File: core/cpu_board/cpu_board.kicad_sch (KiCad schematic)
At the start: 57 parts, among them J1 Data Low, J10 Cycle control, J11 CPU status, J12 CPU control, J13 Power, J2 Data High, J3 Address Low, J4 Address Mid, J5 Address High, J6 JTAG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

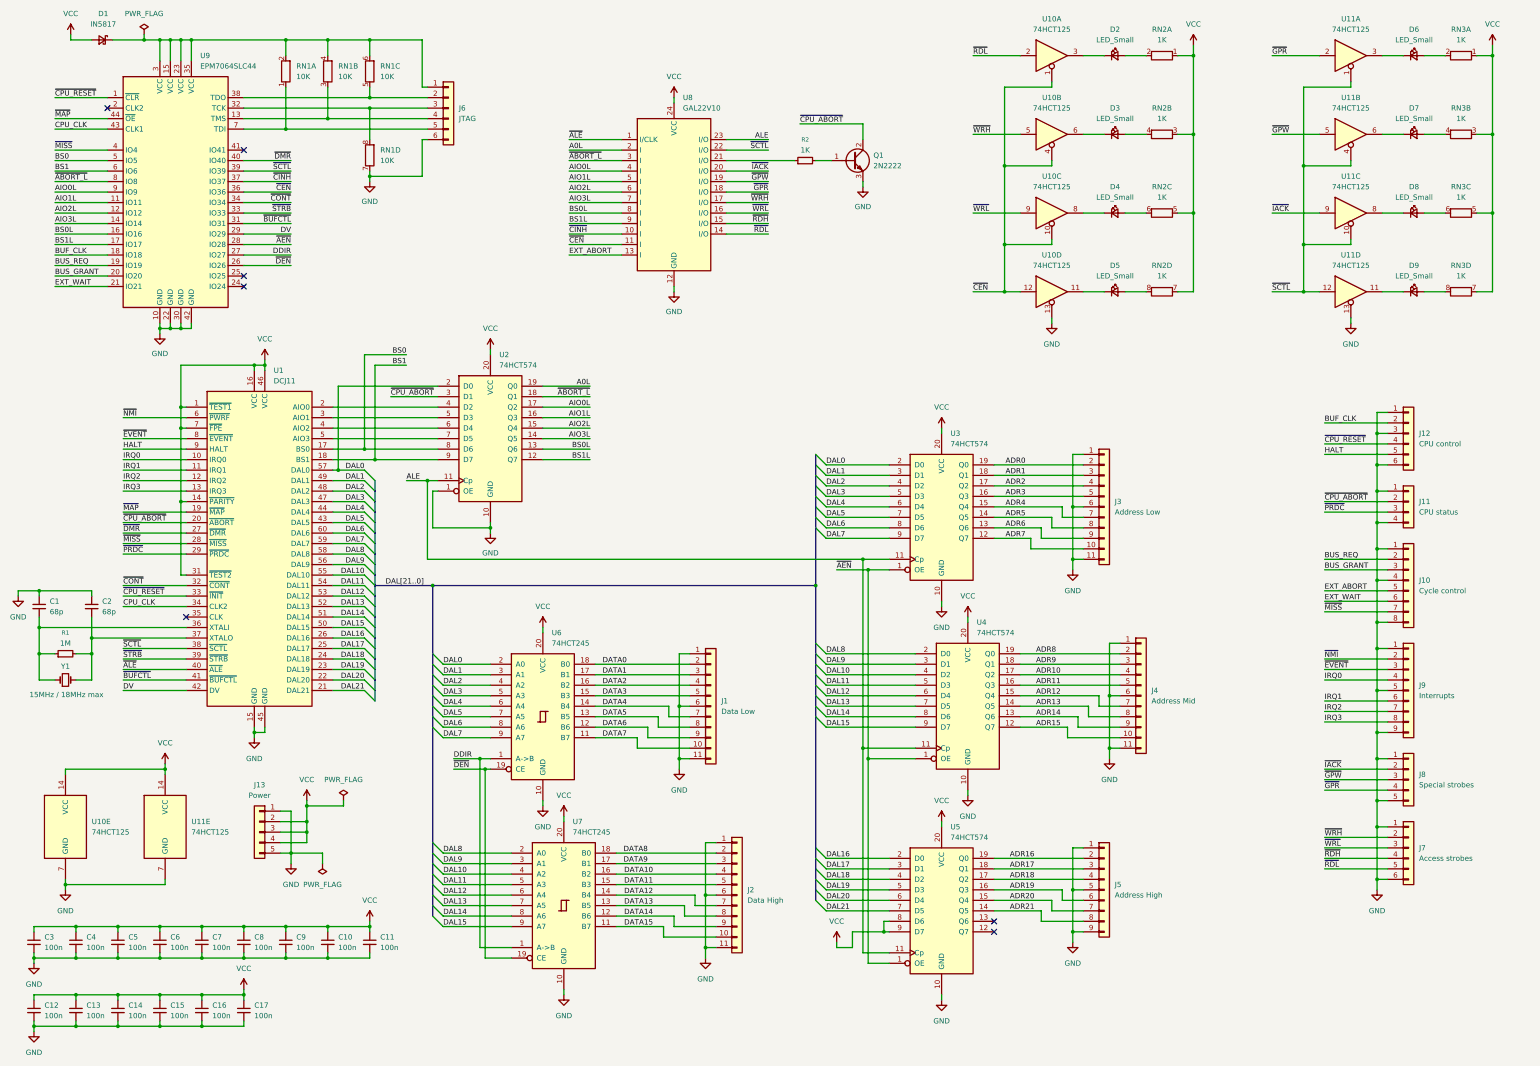
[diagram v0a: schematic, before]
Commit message: Fix: no need to expose CPU's abort signal to frontpanel
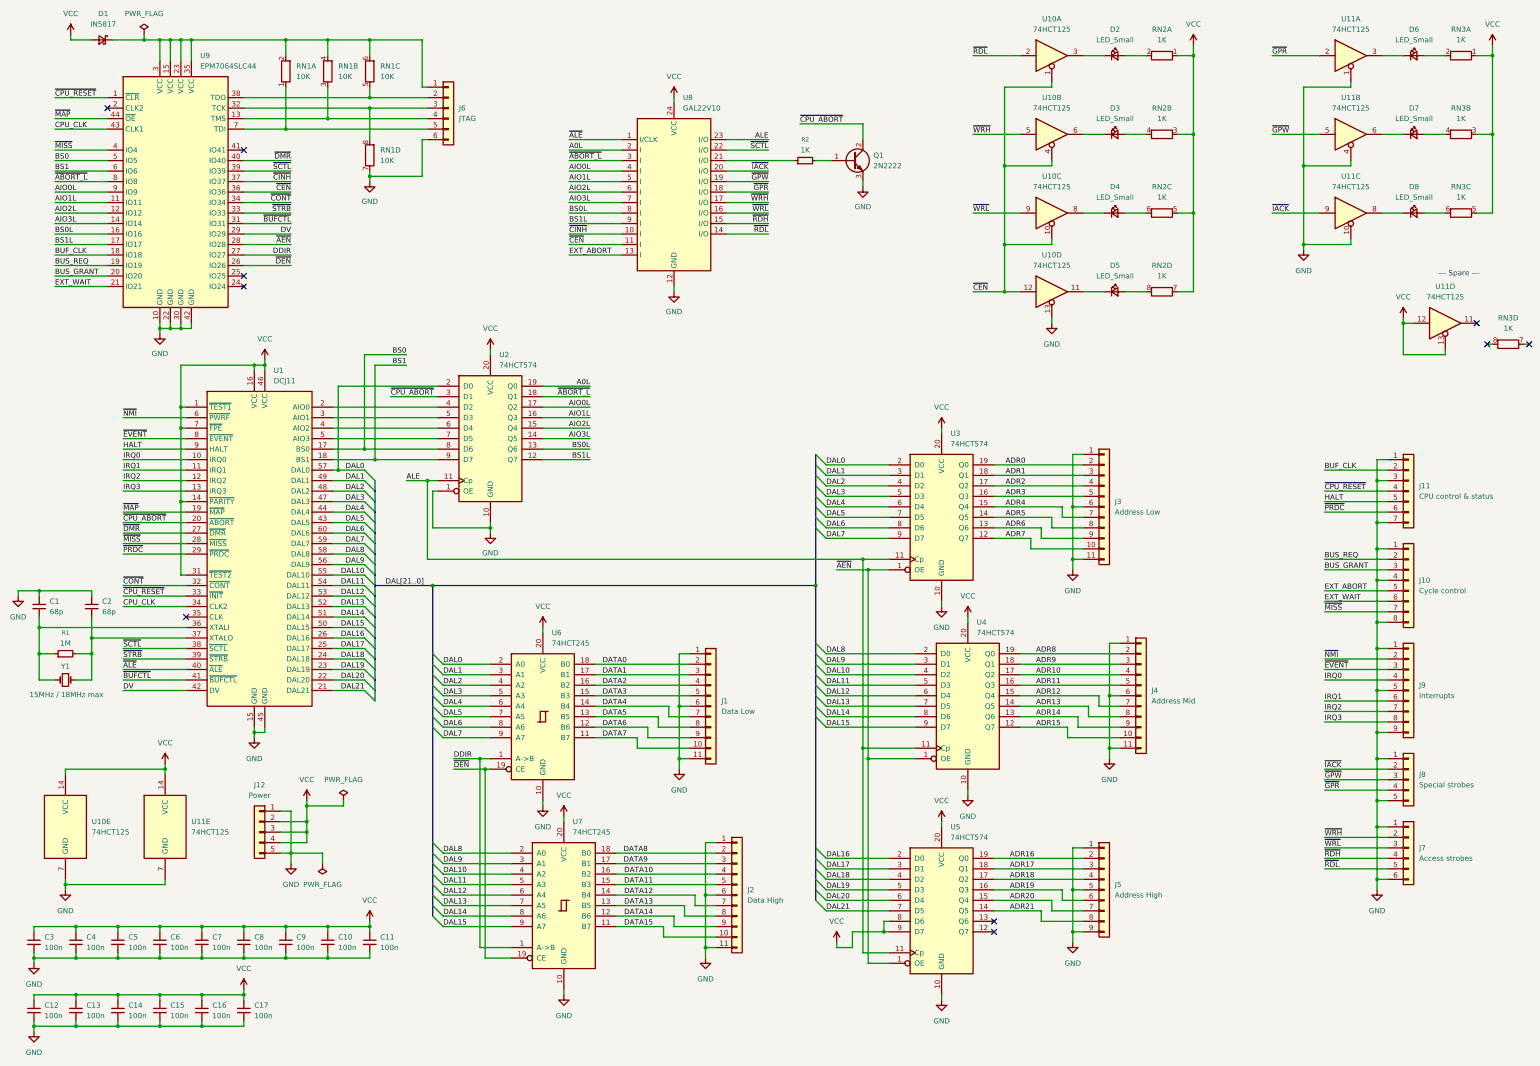
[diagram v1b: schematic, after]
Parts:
- removed D9: LED_Small, symbol Device:LED_Small
- removed J11: CPU status, symbol Connector_Generic:Conn_01x04
- J11: renamed from J12; value CPU control -> CPU control & status; symbol Connector_Generic:Conn_01x06 -> Connector_Generic:Conn_01x07
- renumbered J13 to J12
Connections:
- net GND: now also J11.7 (Pin_7), U11.1, U11.10, U11.4; no longer J11.6 (Pin_6), U11.13
- net VCC: now also U11.12, U11.13; no longer RN3.7 (R4.1)
- net ~{PRDC}: now also J11.6 (Pin_6)
- net ~{SCTL}: no longer U11.1, U11.10, U11.12, U11.4
- no-connect marks 7 -> 10
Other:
- note added: "--- Spare ---"
- moved on the sheet: RN3D, U11D
